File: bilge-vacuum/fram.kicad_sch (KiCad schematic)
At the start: 4 parts, among them U14 FM25V20A

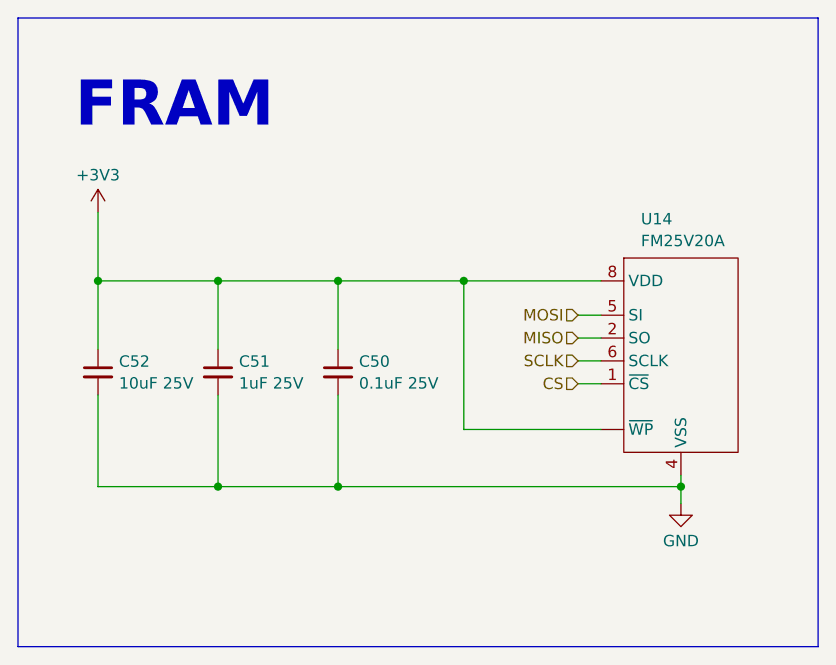
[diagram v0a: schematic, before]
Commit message: Assign the bulk of parts, some passives still need custom footprints.
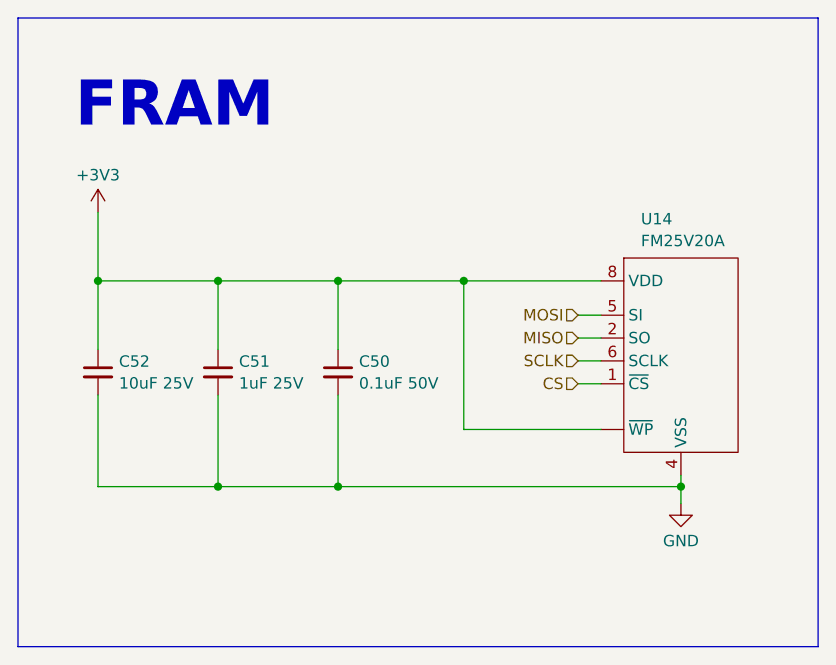
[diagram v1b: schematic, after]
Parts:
- C50: value 0.1uF 25V -> 0.1uF 50V; footprint (none) -> Capacitor_SMD:C_0805_2012Metric
- C51: footprint (none) -> Capacitor_SMD:C_0805_2012Metric
- C52: footprint (none) -> Capacitor_SMD:C_1206_3216Metric
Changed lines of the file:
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@@
       (effects (font (size 1.27 1.27)) (justify left))
     )
-    (property "Value" "0.1uF 25V" (at 56.9341 59.6384 0)
+    (property "Value" "0.1uF 50V" (at 56.9341 59.6384 0)
       (effects (font (size 1.27 1.27)) (justify left))
     )
-    (property "Footprint" "" (at 54.61 58.42 0)
+    (property "Footprint" "Capacitor_SMD:C_0805_2012Metric" (at 54.61 58.42 0)
       (effects (font (size 1.27 1.27)) hide)
     )
@@
       (effects (font (size 1.27 1.27)) (justify left))
     )
-    (property "Footprint" "" (at 27.94 58.42 0)
+    (property "Footprint" "Capacitor_SMD:C_1206_3216Metric" (at 27.94 58.42 0)
       (effects (font (size 1.27 1.27)) hide)
     )
@@
       (effects (font (size 1.27 1.27)) (justify left))
     )
-    (property "Footprint" "" (at 41.275 58.42 0)
+    (property "Footprint" "Capacitor_SMD:C_0805_2012Metric" (at 41.275 58.42 0)
       (effects (font (size 1.27 1.27)) hide)
     )

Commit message: bilge vac 1v0
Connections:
- net +3V3: now also U14.3 (~{WP}); no longer U14. (~{WP})
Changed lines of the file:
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@@
       (effects (font (size 1.27 1.27)) hide)
     )
-    (pin "")
     (pin "1")
     (pin "2")
+    (pin "3")
     (pin "4")
     (pin "5")

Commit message: Fixes
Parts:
- C52: value 10uF 25V -> 10uF 50V
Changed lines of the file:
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@@
       (effects (font (size 1.27 1.27)) (justify left))
     )
-    (property "Value" "10uF 25V" (at 30.2641 59.6384 0)
+    (property "Value" "10uF 50V" (at 30.2641 59.6384 0)
       (effects (font (size 1.27 1.27)) (justify left))
     )
